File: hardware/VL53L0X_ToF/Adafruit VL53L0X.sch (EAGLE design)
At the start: 17 parts, among them Q1 BSS138, Q2 BSS138, U1 VL53L0X, U2 MIC5225_2.8V

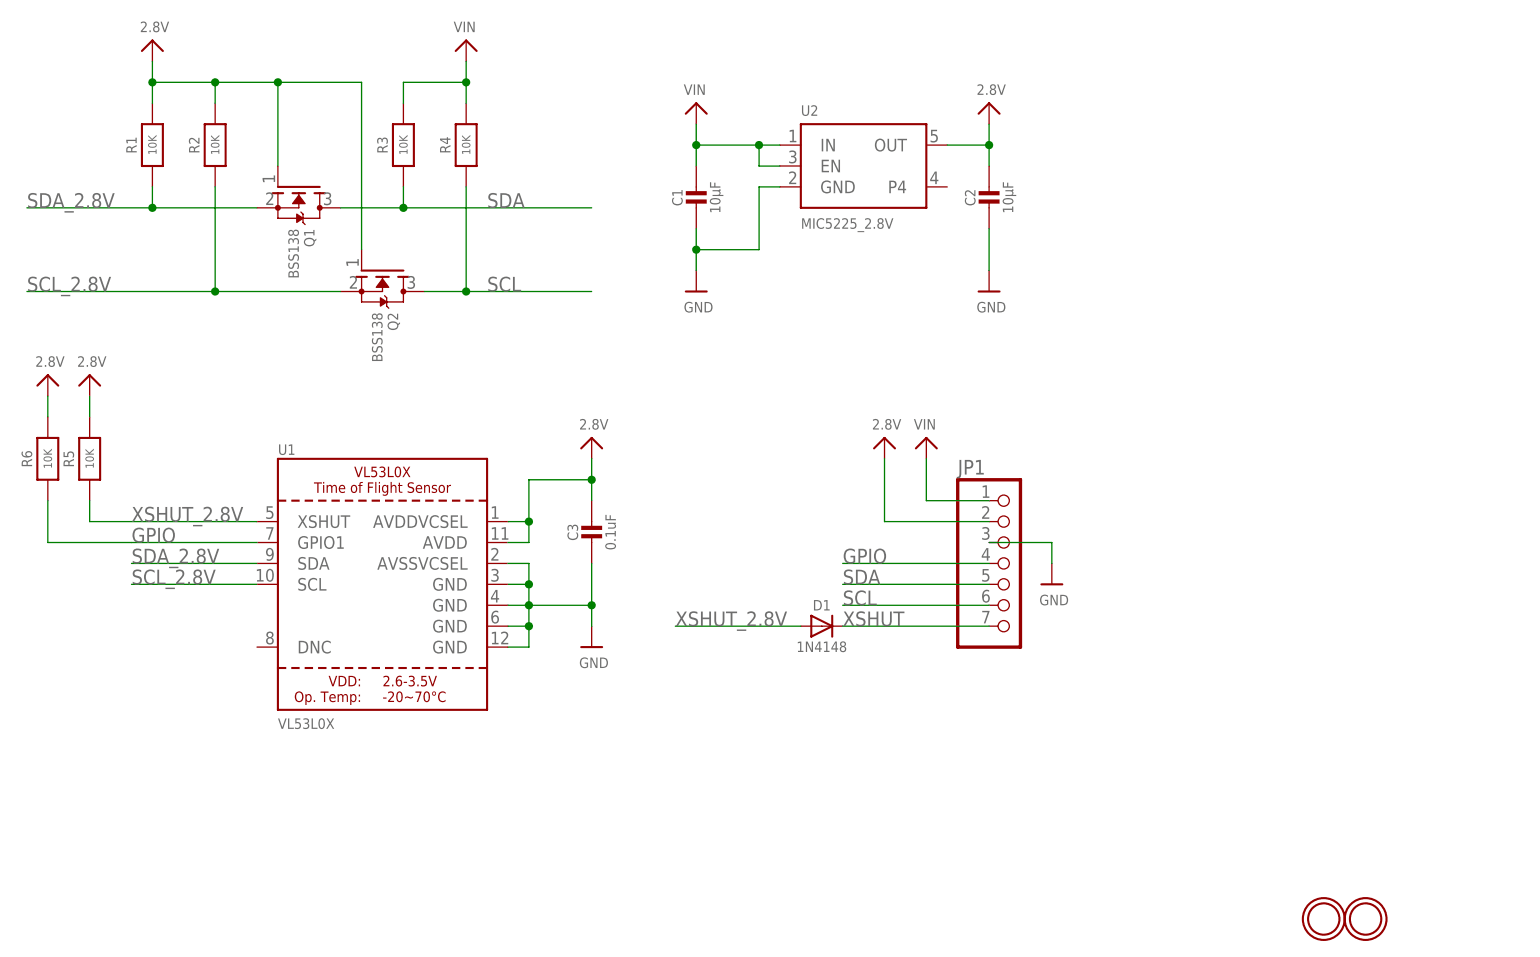
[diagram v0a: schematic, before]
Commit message: revert to original design by adafruit
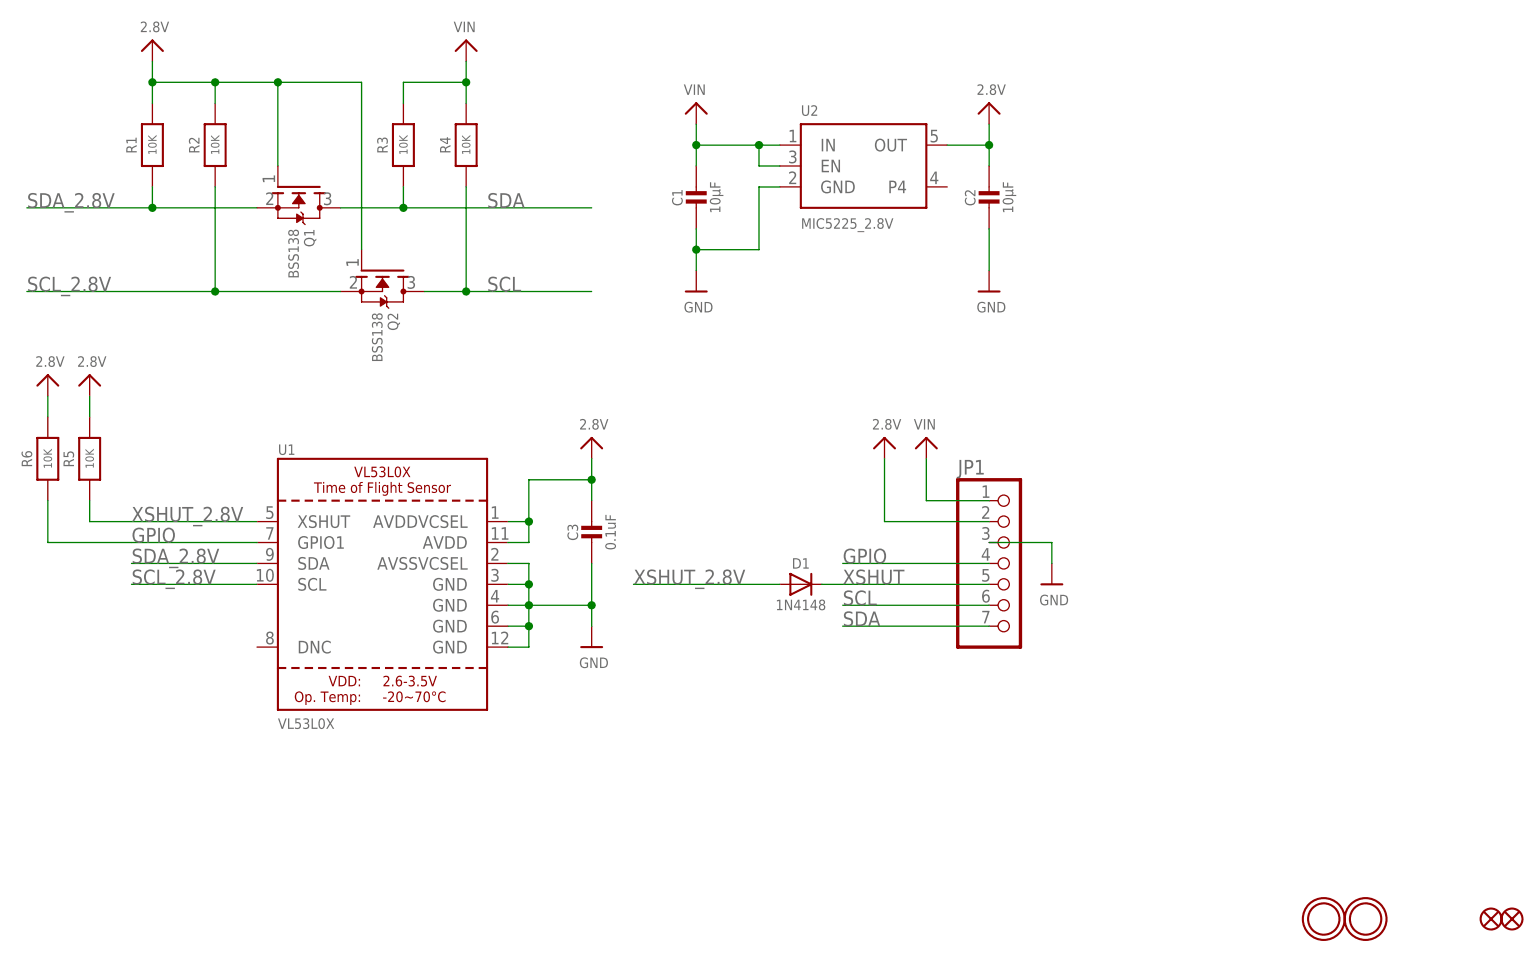
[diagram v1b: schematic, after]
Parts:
- added FID2, FID3: FIDUCIAL"", microbuilder:FIDUCIAL""
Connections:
- net SDA: now also JP1.7; no longer JP1.5
- net XSHUT: now also JP1.5; no longer JP1.7
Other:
- moved on the sheet: D1

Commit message: Trading off PCB design to Binit
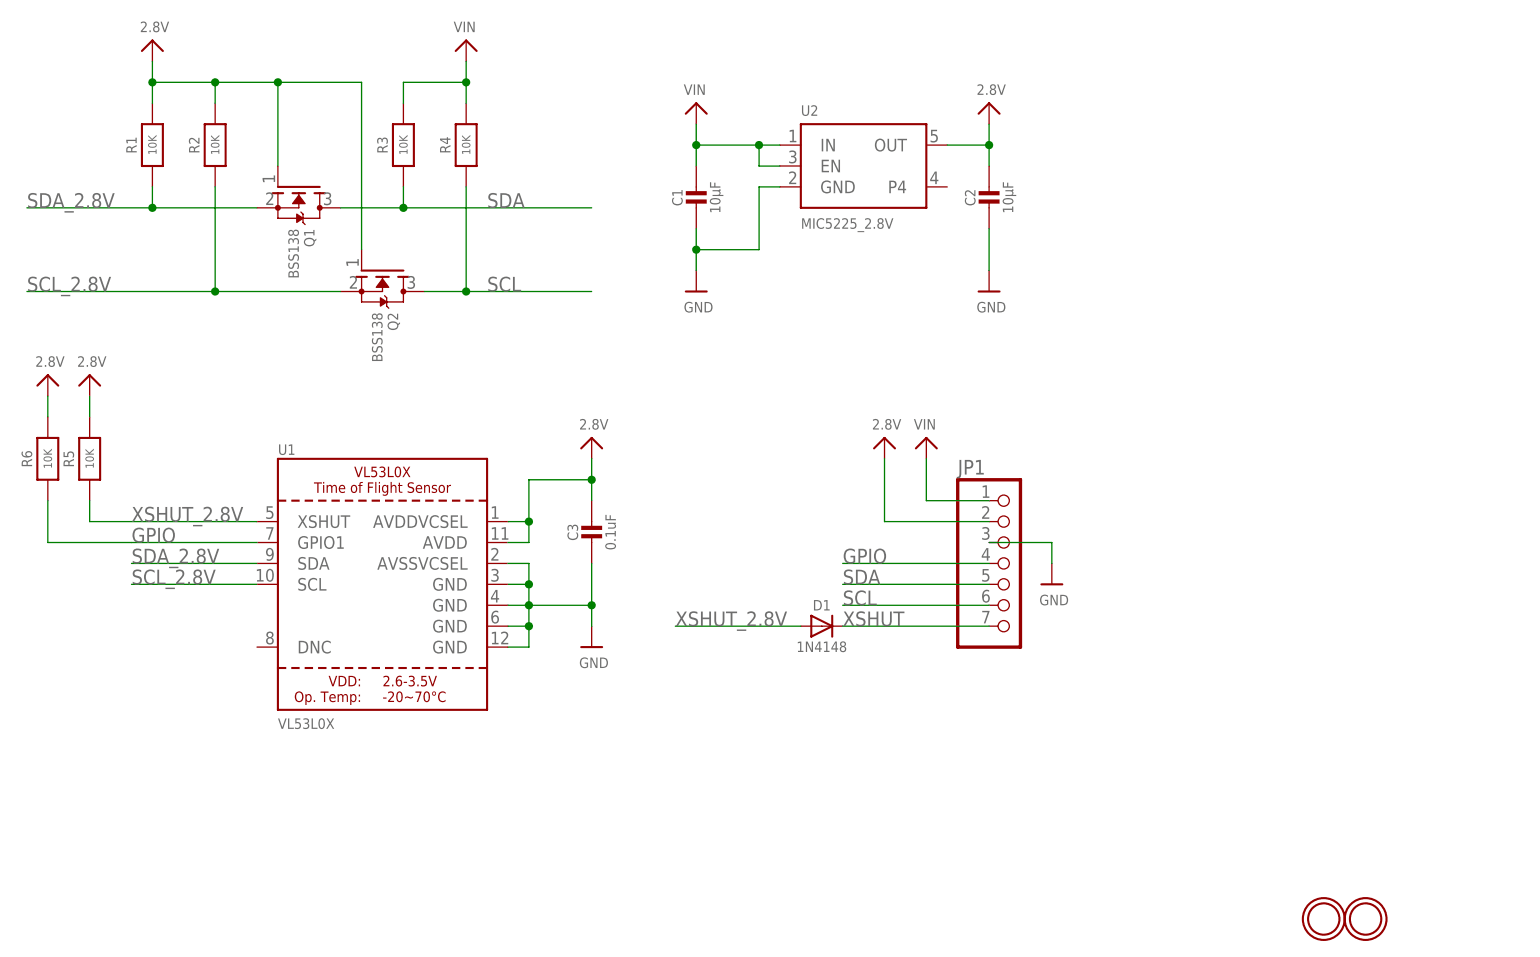
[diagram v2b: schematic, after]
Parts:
- removed FID2, FID3: FIDUCIAL"", microbuilder:FIDUCIAL""
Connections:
- net SDA: now also JP1.5; no longer JP1.7
- net XSHUT: now also JP1.7; no longer JP1.5
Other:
- moved on the sheet: D1
